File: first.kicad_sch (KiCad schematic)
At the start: 48 parts, among them J1 Conn_01x02_Socket, J10 Conn_01x02_Socket, J11 USB_C_Receptacle_USB2.0_16P, J12 Conn_01x03_Socket, J13 Conn_01x02_Socket, J14 Conn_01x02_Socket, J2 Conn_01x03_Socket, J3 Conn_01x03_Socket, J4 Conn_01x03_Socket, J5 Conn_01x03_Socket, J6 Conn_01x03_Socket, J7 Conn_01x03_Socket, J8 Conn_01x03_Socket, J9 Conn_01x03_Socket, SW1 SW_Push, SW3 SW_Wuerth_450301014042, U1 STM32F446RETx, U2 MCP2561-E-SN, U3 CH340E, U4 BD33FC0FP

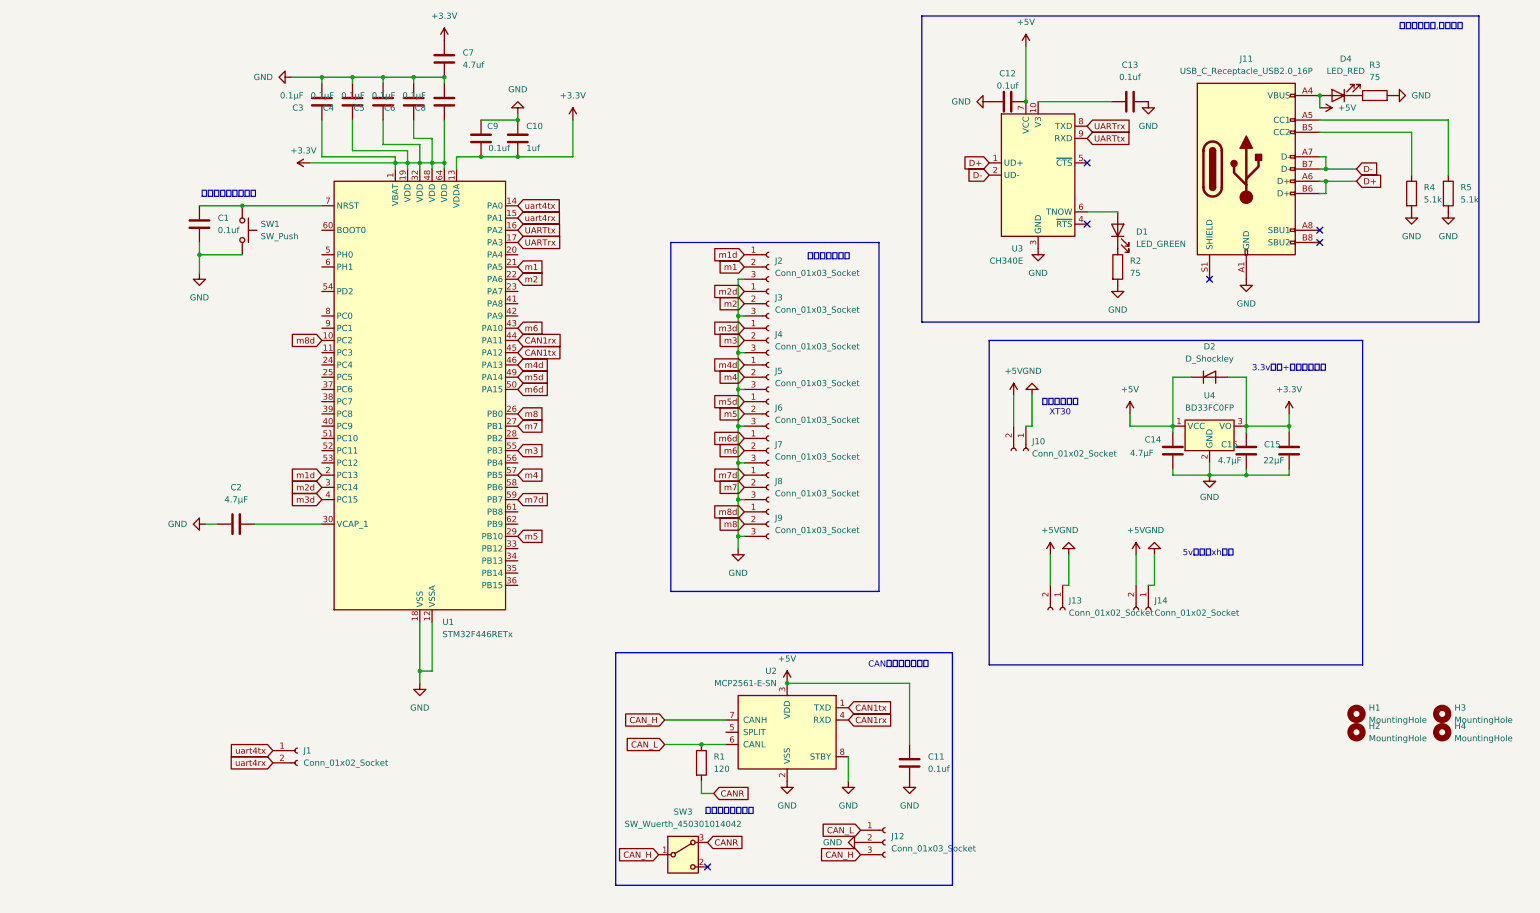
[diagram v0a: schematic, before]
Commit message: mcpモジュールの変更、stlinkV3の追加
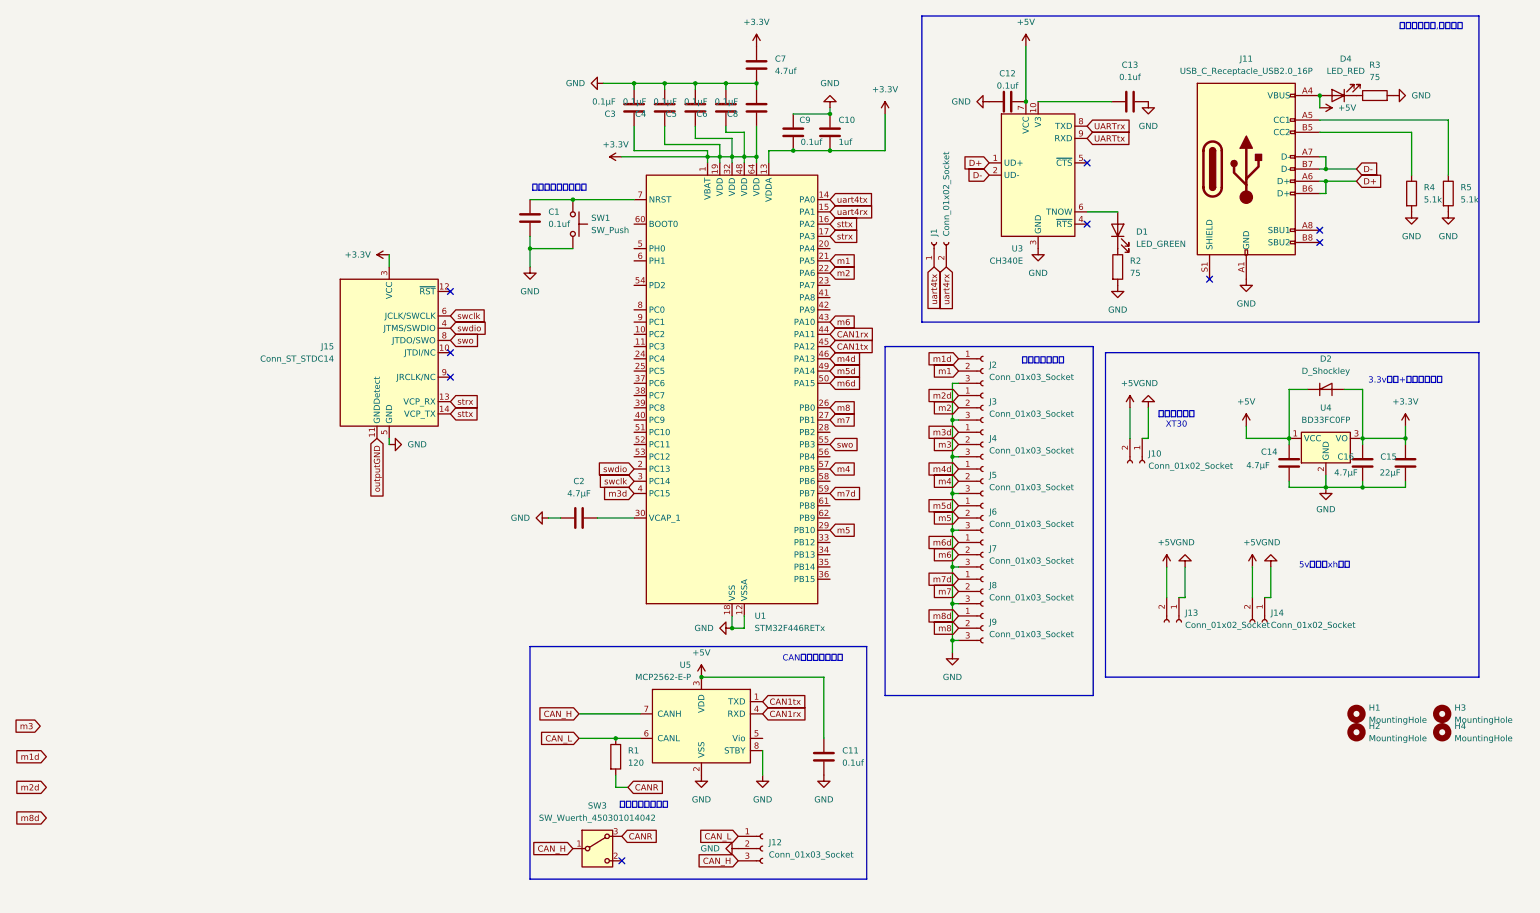
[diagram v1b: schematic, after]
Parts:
- removed U2: MCP2561-E-SN, Package_SO:SOIC-8_3.9x4.9mm_P1.27mm, symbol Interface_CAN_LIN:MCP2561-E-SN
- added J15: Conn_ST_STDC14, Connector_IDC:IDC-Header_2x07_P2.54mm_Vertical, symbol Connector:Conn_ST_STDC14
- added U5: MCP2562-E-P, Package_DIP:DIP-8_W7.62mm, symbol Interface_CAN_LIN:MCP2562-E-P
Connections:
- net +3.3V: now also J15.3 (VCC)
- net +5V: now also U5.3 (VDD)
- net CAN1rx: now also U5.4 (RXD)
- net CAN1tx: now also U5.1 (TXD)
- net CAN_H: now also U5.7 (CANH)
- net CAN_L: now also U5.6 (CANL)
- net GND: now also J15.5 (GND), J15.7 (GND), U5.2 (VSS), U5.8 (STBY)
- net UARTrx: no longer U1.17 (PA3)
- net UARTtx: no longer U1.16 (PA2)
- net m1d: no longer U1.2 (PC13)
- net m2d: no longer U1.3 (PC14)
- net m3: no longer U1.55 (PB3)
- net m8d: no longer U1.10 (PC2)
- new net outputGND: J15.11 (GNDDetect)
- new net strx: J15.13 (VCP_RX), U1.17 (PA3)
- new net sttx: J15.14 (VCP_TX), U1.16 (PA2)
- new net swclk: J15.6 (JCLK/SWCLK), U1.3 (PC14)
- new net swdio: J15.4 (JTMS/SWDIO), U1.2 (PC13)
- new net swo: J15.8 (JTDO/SWO), U1.55 (PB3)
- no-connect marks 6 -> 9
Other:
- moved on the sheet: C1, C10, C11, C14, C15, C16, C2, C3, C4, C5, C6, C7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

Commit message: canモジュールの配線の変更、UART書き込み回路の削除
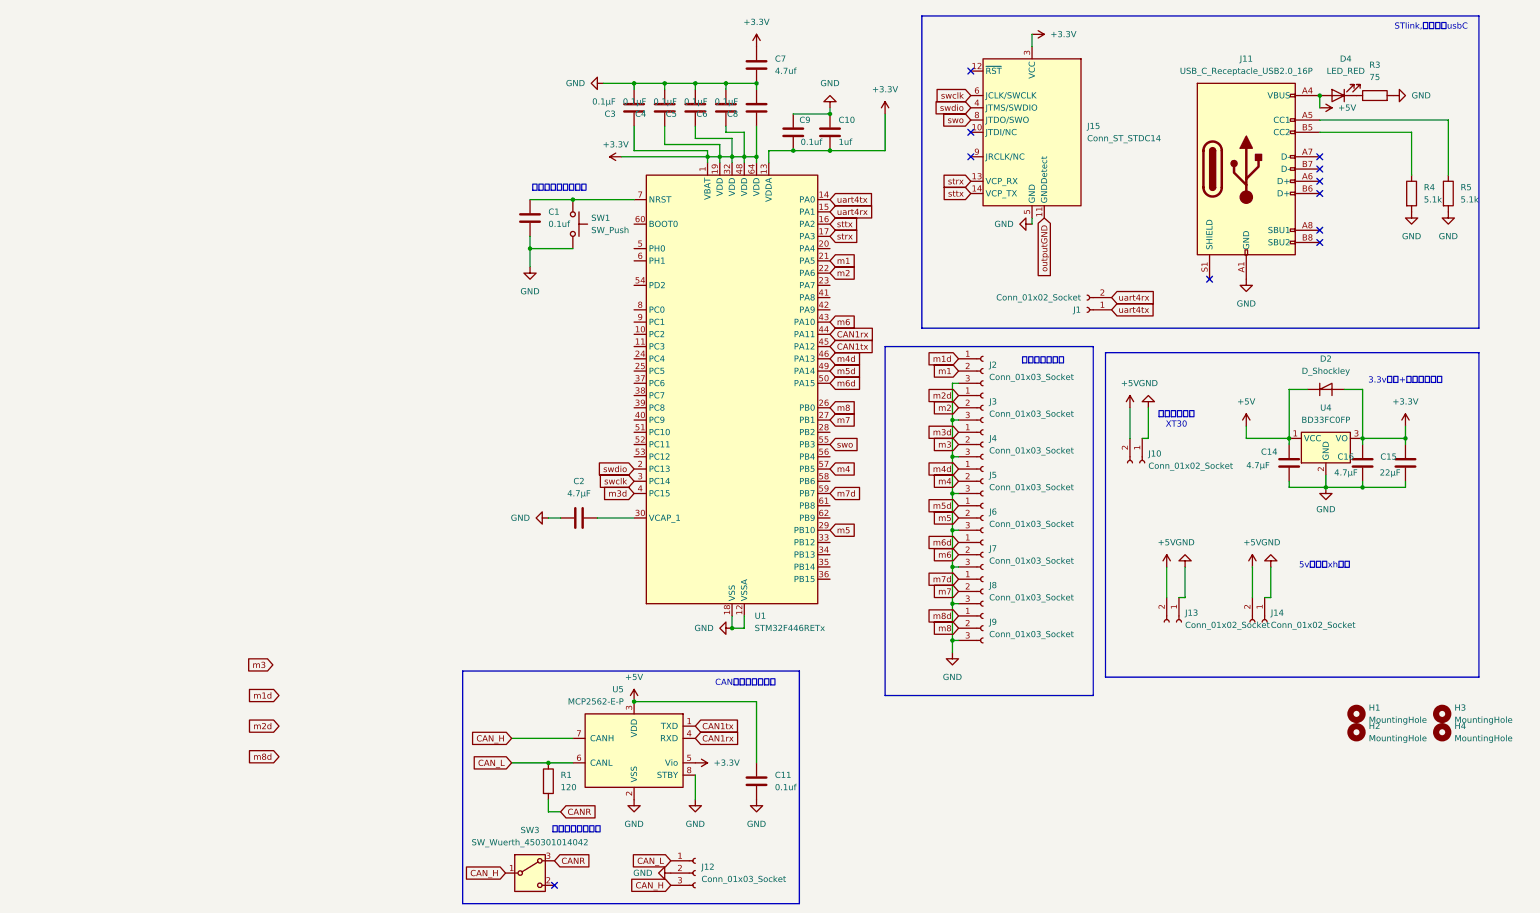
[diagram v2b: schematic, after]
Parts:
- removed C12, C13: 0.1uf, Capacitor_SMD:C_0603_1608Metric_Pad1.08x0.95mm_HandSolder, symbol Device:C
- removed D1: LED_GREEN, Diode_SMD:D_0603_1608Metric_Pad1.05x0.95mm_HandSolder, symbol Device:LED
- removed R2: 75, Resistor_SMD:R_0603_1608Metric_Pad0.98x0.95mm_HandSolder, symbol Device:R
- removed U3: CH340E, Package_SO:MSOP-10_3x3mm_P0.5mm, symbol Interface_USB:CH340E
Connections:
- net +3.3V: now also U5.5 (Vio)
- net D+: no longer names the net of J11.A6 (D+)
- net D+: no longer J11.B6 (D+)
- net D-: no longer names the net of J11.A7 (D-)
- net D-: no longer J11.B7 (D-)
- no-connect marks 9 -> 11
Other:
- note added: "STlink,電源供給usbC"
- note removed: "シリアル通信,書き込み"
- moved on the sheet: C11, J1, J12, J15, R1, SW3, U5

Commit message: a
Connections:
- net CAN1rx: now also U1.61 (PB8); no longer U1.44 (PA11)
- net CAN1tx: now also U1.62 (PB9); no longer U1.45 (PA12)
- net m1: no longer U1.21 (PA5)
- net m2: no longer U1.22 (PA6)
- net m3d: no longer U1.4 (PC15)
- net m4: no longer U1.57 (PB5)
- net m4d: no longer U1.46 (PA13)
- net m5: no longer U1.29 (PB10)
- net m5d: no longer U1.49 (PA14)
- net m6: no longer U1.43 (PA10)
- net m6d: no longer U1.50 (PA15)
- net m7: no longer U1.27 (PB1)
- net m7d: no longer U1.59 (PB7)
- net m8: no longer U1.26 (PB0)
- net swclk: now also U1.49 (PA14); no longer U1.3 (PC14)
- net swdio: now also U1.46 (PA13); no longer U1.2 (PC13)
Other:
- moved on the sheet: C11, J12, J2, J3, J4, J5, J6, J7, J8, J9, R1, SW3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

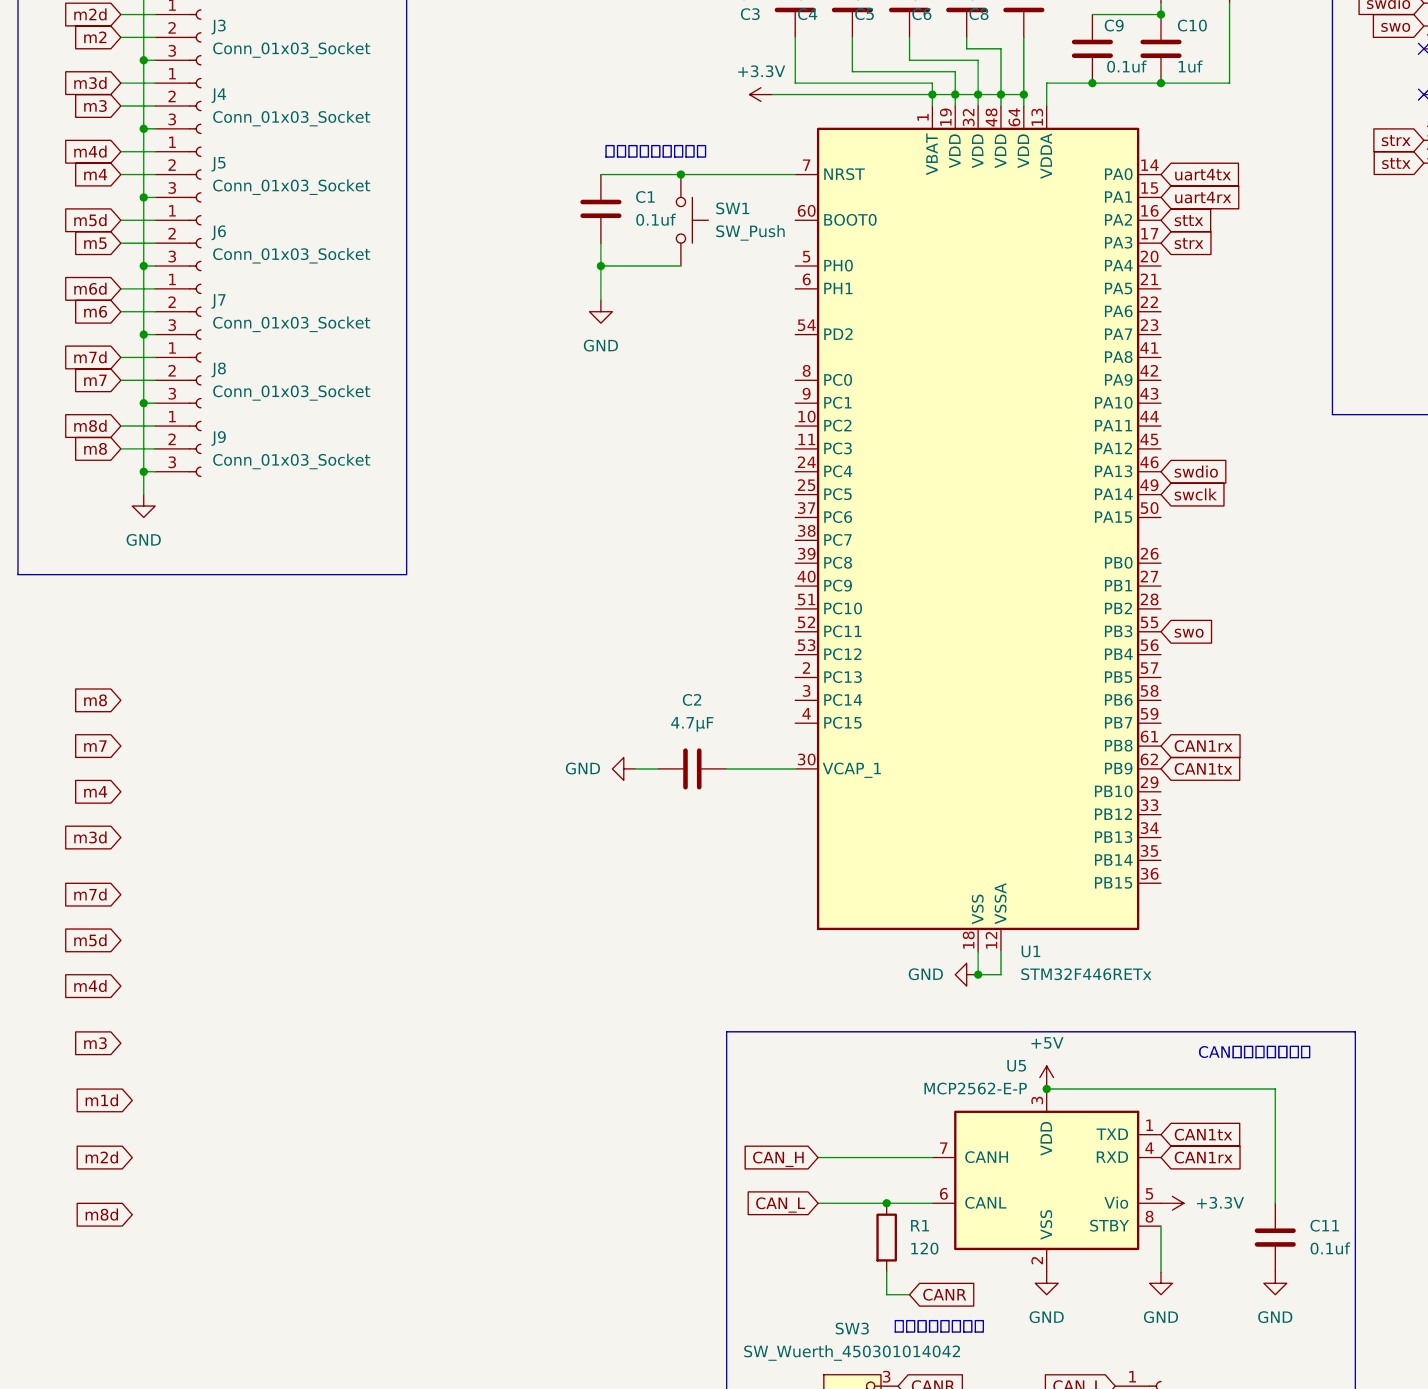
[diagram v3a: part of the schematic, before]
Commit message: デバッグ用LEDの追加,モーター用出力の追加など
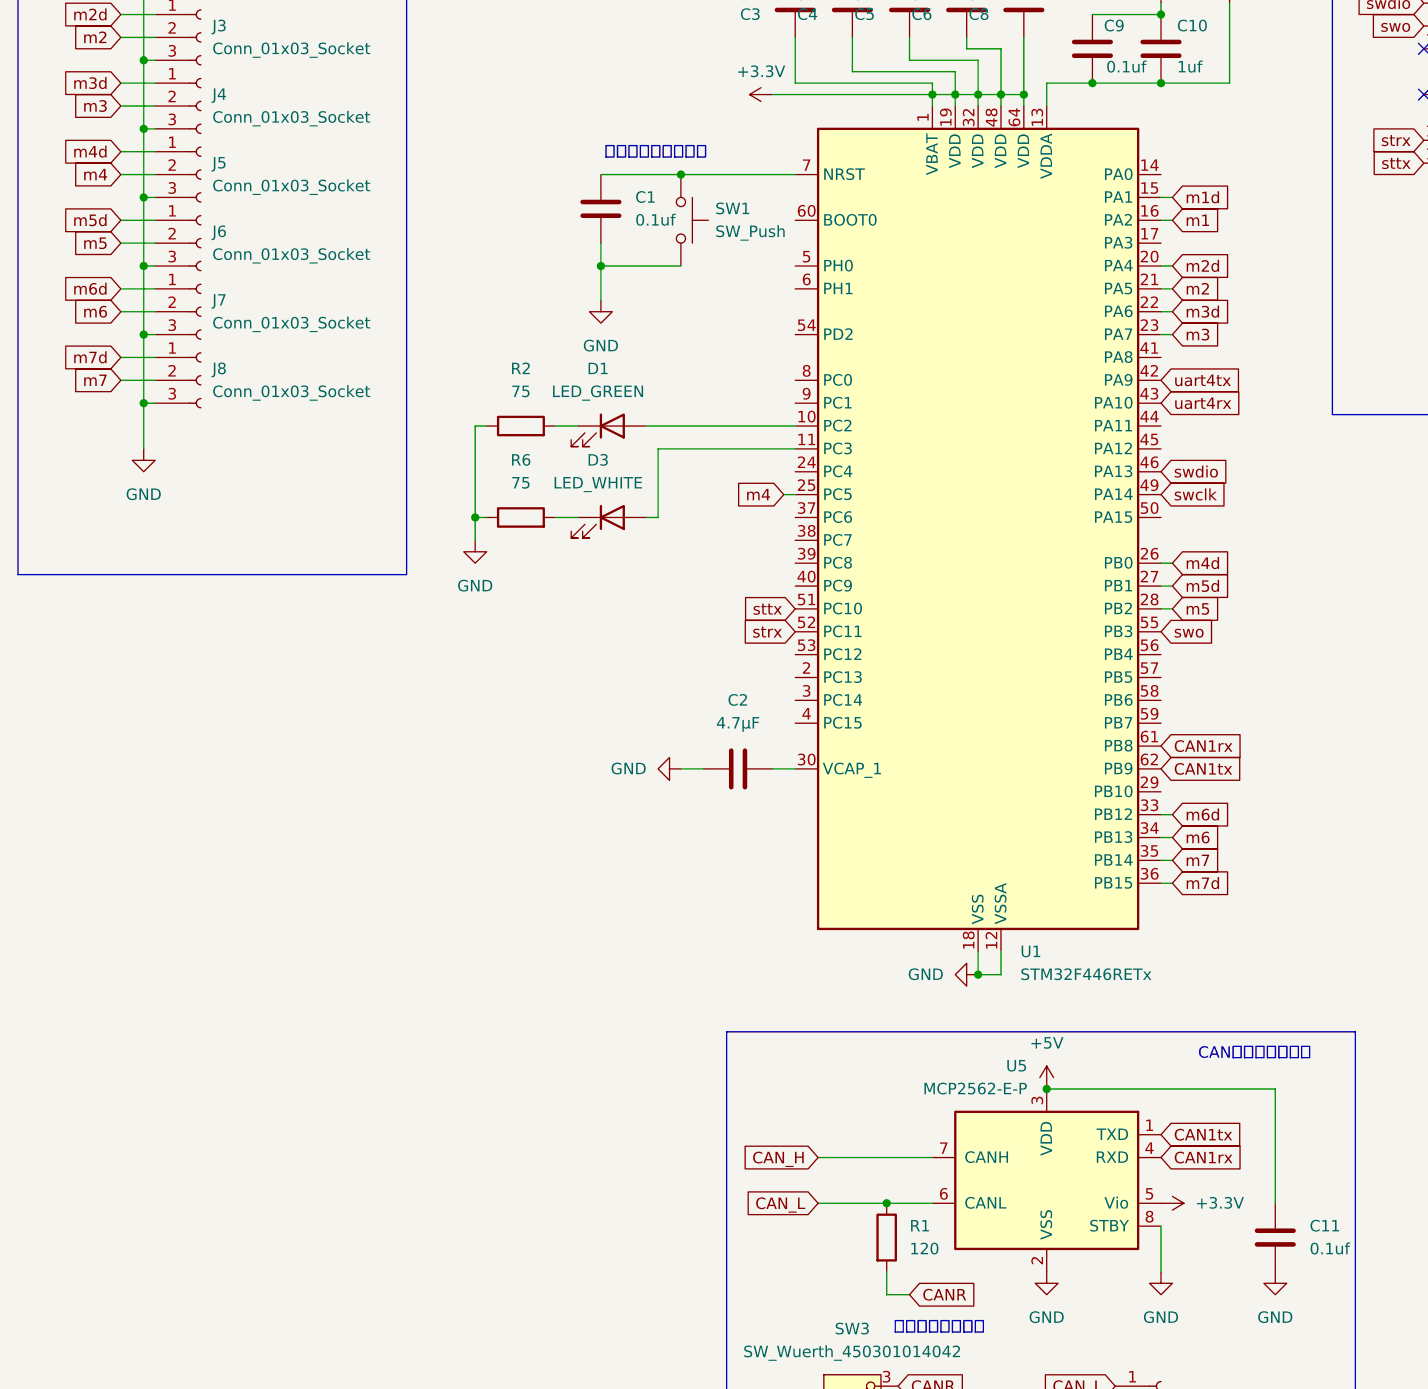
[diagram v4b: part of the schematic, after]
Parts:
- removed J9: Conn_01x03_Socket, Connector_JST:JST_XH_S3B-XH-A-1_1x03_P2.50mm_Horizontal, symbol Connector:Conn_01x03_Socket
- added D1: LED_GREEN, Diode_SMD:D_0603_1608Metric_Pad1.05x0.95mm_HandSolder, symbol Device:LED
- added D3: LED_WHITE, Diode_SMD:D_0603_1608Metric_Pad1.05x0.95mm_HandSolder, symbol Device:LED
- added R2, R6: 75, Resistor_SMD:R_0603_1608Metric_Pad0.98x0.95mm_HandSolder, symbol Device:R
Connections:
- net GND: now also R2.1, R6.1
- net m1: now also U1.16 (PA2)
- net m1d: now also U1.15 (PA1)
- net m2: now also U1.21 (PA5)
- net m2d: now also U1.20 (PA4)
- net m3: now also U1.23 (PA7)
- net m3d: now also U1.22 (PA6)
- net m4: now also U1.25 (PC5)
- net m4d: now also U1.26 (PB0)
- net m5: now also U1.28 (PB2)
- net m5d: now also U1.27 (PB1)
- net m6: now also U1.34 (PB13)
- net m6d: now also U1.33 (PB12)
- net m7: now also U1.35 (PB14)
- net m7d: now also U1.36 (PB15)
- net strx: now also U1.52 (PC11); no longer U1.17 (PA3)
- net sttx: now also U1.51 (PC10); no longer U1.16 (PA2)
- net uart4rx: now also U1.43 (PA10); no longer U1.15 (PA1)
- net uart4tx: now also U1.42 (PA9); no longer U1.14 (PA0)
- net at U1.10 (PC2): now also D1.2 (A)
- net at U1.11 (PC3): now also D3.2 (A)
- new net: D3.1 (K), R6.2
- new net: D1.1 (K), R2.2
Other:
- moved on the sheet: C2
